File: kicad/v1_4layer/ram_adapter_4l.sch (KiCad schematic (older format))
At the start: 5 parts, among them J1 Conn_01x16_Male, J2 Conn_01x16_Male, U1 IS61C5128AL-10KLI

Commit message: Extended SOJ pads by 0.2mm
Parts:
- U1: footprint Package_SO:SOJ-36_10.16x23.49mm_P1.27mm -> footprints:SOJ-36_10.16x23.49mm_P1.27mm
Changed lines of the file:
@@
 F 0 "U1" H 5700 5281 50  0000 C CNN
 F 1 "IS61C5128AL-10KLI" H 5700 5190 50  0000 C CNN
-F 2 "Package_SO:SOJ-36_10.16x23.49mm_P1.27mm" H 5200 4950 50  0001 C CNN
+F 2 "footprints:SOJ-36_10.16x23.49mm_P1.27mm" H 5200 4950 50  0001 C CNN
 F 3 "http://www.issi.com/WW/pdf/61-64C5128AL.pdf" H 5700 3800 50  0001 C CNN
 	1    5700 3800

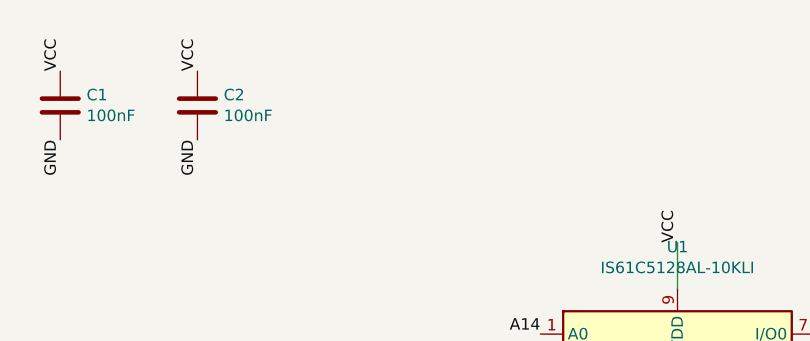
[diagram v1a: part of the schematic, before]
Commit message: Added ground points
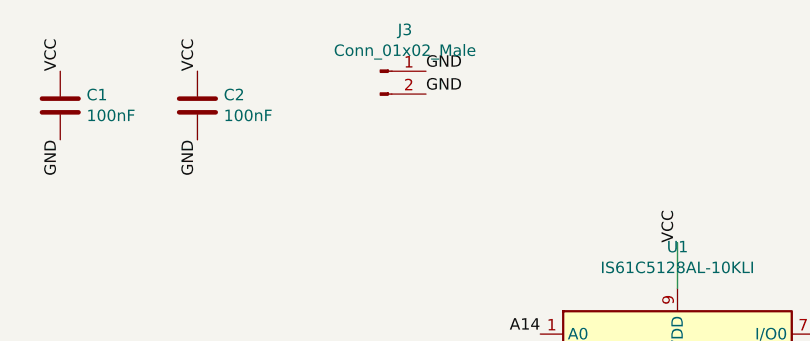
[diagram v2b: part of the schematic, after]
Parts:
- added J3: Conn_01x02_Male, Connector_PinHeader_2.54mm:PinHeader_1x02_P2.54mm_Vertical, symbol Connector:Conn_01x02_Male
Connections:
- net GND: now also J3.1 (Pin_1), J3.2 (Pin_2)
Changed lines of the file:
@@
 Text Label 5100 3700 2    50   ~ 0
 A9
+Text Label 4600 1550 0    50   ~ 0
+GND
+Text Label 4600 1650 0    50   ~ 0
+GND
+$Comp
+L Connector:Conn_01x02_Male J3
+U 1 1 5F9790CB
+P 4400 1550
+F 0 "J3" H 4508 1731 50  0000 C CNN
+F 1 "Conn_01x02_Male" H 4508 1640 50  0000 C CNN
+F 2 "Connector_PinHeader_2.54mm:PinHeader_1x02_P2.54mm_Vertical" H 4400 1550 50  0001 C CNN
+F 3 "~" H 4400 1550 50  0001 C CNN
+	1    4400 1550
+	1    0    0    -1
+$EndComp
 $EndSCHEMATC
